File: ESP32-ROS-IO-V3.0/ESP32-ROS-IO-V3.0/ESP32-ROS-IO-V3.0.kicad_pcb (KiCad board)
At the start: 2 copper layers, 99.1 x 99.1 mm, 64 parts, among them J1 Conn_01x19_Socket, J12 XT60-M, J13 XT60-M, J2 Conn_01x19_Socket, J3 Conn_01x19_Socket, J4 Conn_01x19_Socket, SW1 SW1, SW2 SW2, SW3 SW3, SW4 SW4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

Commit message: 名前変更、整理
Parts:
- removed G***, G***5, G***6: LOGO, LOGO
- removed MD1: MD1, Connector_PinHeader_2.54mm:PinHeader_1x04_P2.54mm_Vertical
- removed MD2: MD2, Connector_PinHeader_2.54mm:PinHeader_1x04_P2.54mm_Vertical
- removed MD3: MD3, Connector_PinHeader_2.54mm:PinHeader_1x04_P2.54mm_Vertical
- removed MD4: MD4, Connector_PinHeader_2.54mm:PinHeader_1x04_P2.54mm_Vertical
- removed MD5: MD5, Connector_PinHeader_2.54mm:PinHeader_1x04_P2.54mm_Vertical
- removed MD6: MD6, Connector_PinHeader_2.54mm:PinHeader_1x04_P2.54mm_Vertical
- removed MD7: MD7, Connector_PinHeader_2.54mm:PinHeader_1x04_P2.54mm_Vertical
- removed MD8: MD8, Connector_PinHeader_2.54mm:PinHeader_1x04_P2.54mm_Vertical
- removed REF**1, REF**2, REF**3, REF**4: MountingHole_3.2mm_M3, MountingHole:MountingHole_3.2mm_M3
- removed Servo5: Servo5, Connector_JST:JST_XH_B3B-XH-A_1x03_P2.50mm_Vertical
- removed Servo6: Servo6, Connector_JST:JST_XH_B3B-XH-A_1x03_P2.50mm_Vertical
- removed Servo7: Servo7, Connector_JST:JST_XH_B3B-XH-A_1x03_P2.50mm_Vertical
- removed Servo8: Servo8, Connector_JST:JST_XH_B3B-XH-A_1x03_P2.50mm_Vertical
- added J5: Conn_01x02_Pin, Connector_PinSocket_2.54mm:PinSocket_1x19_P2.54mm_Vertical, F.Cu at (228.6, 94.2)
- added J6: Conn_01x02_Pin, Connector_PinSocket_2.54mm:PinSocket_1x19_P2.54mm_Vertical, F.Cu at (232.4, 94.2)
- J12, J13: footprint Connector_AMASS:AMASS_XT60-M_1x02_P7.20mm_Vertical -> XT60PW-M (2):AMASS_XT30PW-F
- moved SW4 159.6 mm to (31.3, 2.88)
- moved J13 149.6 mm to (21.8, 56.0)
- moved SW5 147.0 mm to (31.3, 10.7)
- moved SW6 147.0 mm to (31.3, 18.5)
- moved SW7 147.0 mm to (31.3, 26.3)
- moved SW8 147.0 mm to (31.3, 34.1)
- moved CAN_BUS8 141.2 mm to (12.4, 10.7), turned to 0 degrees
- moved SW1 139.2 mm to (21.9, 26.3)
- moved SW2 139.2 mm to (21.9, 34.1)
- moved SW3 139.2 mm to (21.9, 41.9)
- moved CAN_BUS7 137.9 mm to (12.4, 2.88), turned to 0 degrees
- moved SV7 136.8 mm to (21.9, 18.5), turned to 0 degrees
- moved VMD3/VMD4 136.1 mm to (44.2, 33.0), turned to 0 degrees
- moved SV6 133.9 mm to (21.9, 10.7), turned to 0 degrees
- moved D1 133.2 mm to (59.7, 46.1)
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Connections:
- ENC1 pad 3: GPIO12 -> GPIO19
- ENC1 pad 4: GPIO13 -> GPIO21
- ENC2 pad 3: GPIO14 -> GPIO22
- ENC2 pad 4: GPIO15 -> GPIO23
- ENC3 pad 3: GPIO21 -> GPIO15
- ENC3 pad 4: GPIO22 -> GPIO16
- ENC4 pad 3: GPIO23 -> GPIO17
- ENC4 pad 4: GPIO25 -> GPIO18
- J3 pad 13: GPIO4 -> CAN_TX
- J3 pad 15: GPIO2 -> CAN_RX
- J4 pad 13: GPIO4 -> CAN_TX
- J4 pad 15: GPIO2 -> CAN_RX
- SW1 pad 1: GPIO26 -> GPIO5
- SW2 pad 1: GPIO27 -> GPIO12
- SW3 pad 1: GPIO32 -> GPIO13
- SW4 pad 1: GPIO33 -> GPIO14
- SW5 pad 1: GPIO2 -> GPIO15
- SW6 pad 1: GPIO19 -> GPIO16
- SW7 pad 1: GPIO14 -> GPIO17
- SW8 pad 1: GPIO15 -> GPIO18
- Servo1 pad 1: GPIO16 -> GPIO19
- Servo2 pad 1: GPIO17 -> GPIO21
- Servo3 pad 1: GPIO18 -> GPIO22
- Servo4 pad 1: GPIO19 -> GPIO23
- U1 pad 1: GPIO5 -> CAN_TX
- U1 pad 4: GPIO4 -> CAN_RX
- U2 pad 1: GPIO2 -> GPIO25
- U2 pad 2: GPIO4 -> GPIO26
- U2 pad 3: GPIO5 -> GPIO27
- U2 pad 4: GPIO12 -> GPIO32
- U2 pad 5: GPIO13 -> GPIO33
- U2 pad 6: GPIO14 -> TR6
- U2 pad 7: GPIO15 -> TR6_Bypass_OUT
- VMD1/VMD2 pad 11: GPIO12 -> GPIO15
- VMD1/VMD2 pad 5: GPIO22 -> GPIO12
- VMD1/VMD2 pad 7: GPIO13 -> GPIO16
- VMD1/VMD2 pad 9: GPIO21 -> GPIO5
- VMD3/VMD4 pad 11: GPIO14 -> GPIO17
- VMD3/VMD4 pad 5: GPIO25 -> GPIO14
- VMD3/VMD4 pad 7: GPIO15 -> GPIO18
- VMD3/VMD4 pad 9: GPIO23 -> GPIO13
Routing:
- net (no net): track 0.00 -> 276.3 mm, vias 0 -> 4
- net GPIO2: track 129.3 -> 0.00 mm, vias 1 -> 0
- net GPIO4: track 120.0 -> 0.00 mm, vias 3 -> 0
- net GPIO22: track 203.0 -> 300.9 mm, vias 0 -> 1
- net GPIO18: track 97.9 -> 0.00 mm, vias 1 -> 0
- net GPIO21: track 189.7 -> 274.8 mm, vias 1 -> 2
- net GPIO19: track 153.2 -> 231.8 mm, vias 3 -> 5
- net GPIO23: track 152.3 -> 85.1 mm
- net GPIO13: track 162.0 -> 112.7 mm, vias 1 -> 0
- net GPIO15: track 195.2 -> 233.4 mm
- net GPIO12: track 152.2 -> 114.0 mm
- net GPIO16: track 78.6 -> 49.3 mm, vias 2 -> 1
- net +5V: track 27.0 -> 0.00 mm
- net GPIO17: track 85.1 -> 67.3 mm, vias 1 -> 0
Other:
- board outline removed
- board text removed: "+ GND"
- board text removed: "24V"
- board text removed: "3V G A B"
- board text removed: "5V G P D"
- board text removed: "CAN"
- board text removed: "ESP32-DevKitC V4"
- board text removed: "ESP32-IO-Board-V1.1 2025, NHK-Project, RRST"
- board text removed: "GND +"
- board text removed: "GND GND"
- board text removed: "H L"
- board text removed: "S + GND"
- board text removed: "VSRV"

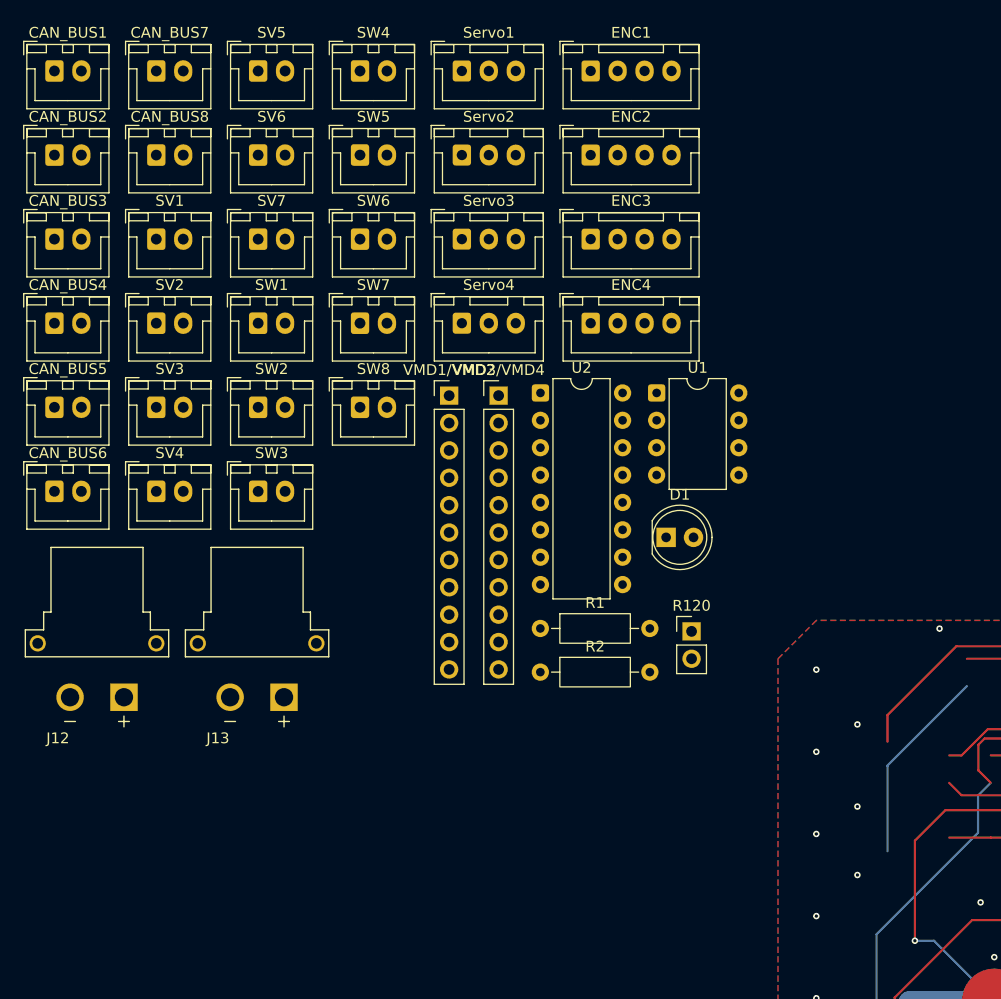
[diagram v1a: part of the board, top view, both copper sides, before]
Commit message: Gerberをzip形式に圧縮、発注したい
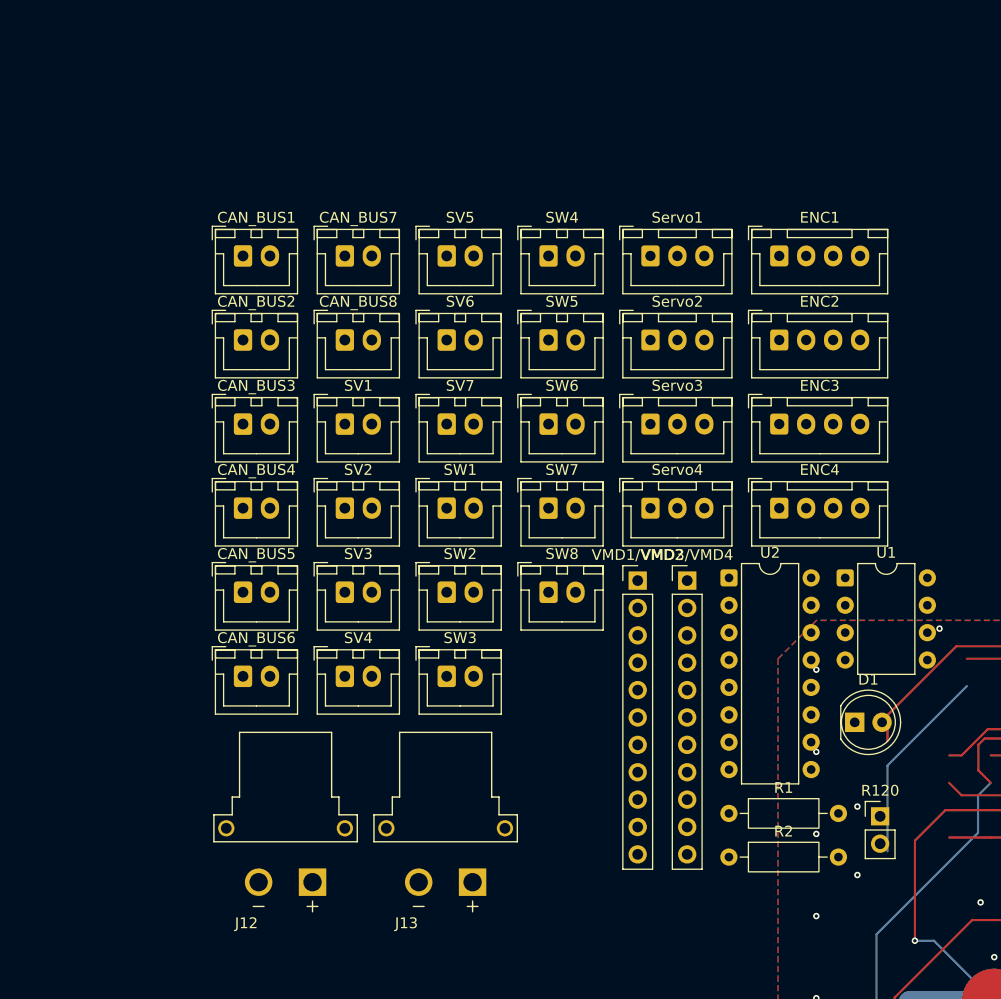
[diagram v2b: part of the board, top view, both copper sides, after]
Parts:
- moved U1 24.5 mm to (76.3, 49.9)
- moved U2 24.5 mm to (65.6, 49.9)
- moved VMD1/VMD2 24.5 mm to (57.1, 50.2)
- moved CAN_BUS7 24.5 mm to (29.9, 20.0)
- moved CAN_BUS8 24.5 mm to (29.9, 27.8)
- moved J12 24.5 mm to (24.4, 73.1)
- moved J13 24.5 mm to (39.3, 73.1)
- moved R1 24.5 mm to (65.5, 71.8)
- moved SV1 24.5 mm to (29.9, 35.6)
- moved SV2 24.5 mm to (29.9, 43.4)
- moved SV3 24.5 mm to (29.9, 51.2)
- moved SV4 24.5 mm to (29.9, 59.0)
- moved SW4 24.5 mm to (48.8, 20.0)
- moved SW5 24.5 mm to (48.8, 27.8)
- moved SW6 24.5 mm to (48.8, 35.6)
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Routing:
- net CANL: track 104.1 -> 32.4 mm
- net 3V3: track 84.0 -> 155.6 mm

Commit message: また変更したよ
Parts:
- removed VMD1/VMD2: VMD1/VMD2, Connector_PinHeader_2.54mm:PinHeader_1x11_P2.54mm_Vertical
- removed VMD3/VMD4: VMD3/VMD4, Connector_PinHeader_2.54mm:PinHeader_1x11_P2.54mm_Vertical
- added J10: XT30UPB-M, XT30UPB-M:AMASS_XT30UPB-M, F.Cu at (81.5, 32.6)
- added J11: XT30UPB-M, XT30UPB-M:AMASS_XT30UPB-M, F.Cu at (81.5, 39.3)
- added J14: XT60-M, XT60-M:AMASS_XT60-M, F.Cu at (83.7, 67.3)
- added J15: XT60-M, XT60-M:AMASS_XT60-M, F.Cu at (83.7, 77.0)
- added J7: Conn_01x04_Socket, Connector_PinSocket_2.54mm:PinSocket_1x04_P2.54mm_Vertical, F.Cu at (20.4, 76.5)
- added J8: XT30UPB-M, XT30UPB-M:AMASS_XT30UPB-M, F.Cu at (81.5, 19.1)
- added J9: XT30UPB-M, XT30UPB-M:AMASS_XT30UPB-M, F.Cu at (81.5, 25.8)
- J12, J13: value XT60-M -> XT30UPB-M; footprint XT60PW-M (2):AMASS_XT30PW-F -> XT30UPB-M:AMASS_XT30UPB-M
- J5, J6: footprint Connector_PinSocket_2.54mm:PinSocket_1x19_P2.54mm_Vertical -> Connector_PinHeader_2.54mm:PinHeader_1x02_P2.54mm_Vertical
- moved J3 206.0 mm to (29.6, 18.0)
- moved J4 205.3 mm to (34.2, 18.0)
- moved J1 191.1 mm to (20.4, 18.0)
- moved J2 183.4 mm to (25.0, 18.0)
- moved J5 153.0 mm to (75.9, 84.1)
- moved J6 152.2 mm to (80.5, 84.1)
- moved J12 63.2 mm to (81.5, 46.1)
- moved U1 58.4 mm to (24.2, 76.2)
- moved D1 58.4 mm to (25.1, 89.6)
- moved Servo4 49.4 mm to (39.9, 89.3)
- moved Servo1 49.4 mm to (39.9, 65.9)
- moved ENC4 49.4 mm to (51.9, 89.3)
- moved ENC1 49.4 mm to (51.9, 65.9)
- moved ENC2 49.4 mm to (51.9, 73.7)
- moved ENC3 49.4 mm to (51.9, 81.5)
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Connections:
- net 5V0 renamed 5V
- J12 pad N: GND -> GPIO17
- J12 pad P: SERVO+ -> GPIO13
- J13 pad N: GND -> GPIO18
- J13 pad P: +24V -> GPIO14
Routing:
- net GND: track 397.4 -> 0.00 mm, vias 111 -> 0
- net GPIO22: track 300.9 -> 0.00 mm, vias 1 -> 0
- net (no net): track 276.3 -> 0.00 mm, vias 4 -> 0
- net GPIO21: track 274.8 -> 0.00 mm, vias 2 -> 0
- net GPIO15: track 233.4 -> 0.00 mm, vias 1 -> 0
- net GPIO19: track 231.8 -> 0.00 mm, vias 5 -> 0
- net GPIO14: track 191.2 -> 0.00 mm, vias 1 -> 0
- net 3V3: track 155.6 -> 0.00 mm, vias 1 -> 0
- net GPIO25: track 155.6 -> 0.00 mm, vias 2 -> 0
- net SERVO+: track 134.2 -> 0.00 mm
- net +24V: track 121.3 -> 0.00 mm
- net GPIO12: track 114.0 -> 0.00 mm, vias 1 -> 0
- net GPIO13: track 112.7 -> 0.00 mm
- net GPIO26: track 108.4 -> 0.00 mm, vias 1 -> 0
- net GPIO27: track 107.6 -> 0.00 mm, vias 1 -> 0
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- removed copper zone on B.Cu, net GND
- removed copper zone on F.Cu, net GND

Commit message: 授業中続きやるよー
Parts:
- moved J3 218.5 mm to (228.6, 108.2)
- moved J1 200.5 mm to (199.4, 108.2)
- moved J4 124.3 mm to (148.1, 67.6)
- moved J2 124.3 mm to (138.9, 67.6)
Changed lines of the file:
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@@
 		)
 		(embedded_fonts no)
+		(model "${KIPRJMOD}/XT30UPB-M/XT30UPB-M.step"
+			(offset
+				(xyz 0 0 0)
+			)
+			(scale
+				(xyz 1 1 1)
+			)
+			(rotate
+				(xyz 90 -180 -180)
+			)
+		)
 	)
 	(footprint "Connector_JST:JST_XH_B2B-XH-A_1x02_P2.50mm_Vertical"
@@
 		)
 		(embedded_fonts no)
+		(model "C:/Users/minio/kicad-ws/MD/MDv3/XT60-M/XT60-M.step"
+			(offset
+				(xyz 0 0 0)
+			)
+			(scale
+				(xyz 1 1 1)
+			)
+			(rotate
+				(xyz 90 -180 -180)
+			)
+		)
 	)
 	(footprint "Connector_JST:JST_XH_B4B-XH-A_1x04_P2.50mm_Vertical"
@@
 		)
 		(embedded_fonts no)
+		(model "C:/Users/minio/kicad-ws/MD/MDv3/XT60-M/XT60-M.step"
+			(offset
+				(xyz 0 0 0)
+			)
+			(scale
+				(xyz 1 1 1)
+			)
+			(rotate
+				(xyz 90 -180 -180)
+			)
+		)
 	)
 	(footprint "Package_DIP:DIP-16_W7.62mm"
@@
 	(footprint "Connector_PinSocket_2.54mm:PinSocket_1x19_P2.54mm_Vertical"
 		(layer "F.Cu")
-		(at 24.96 18.004)
+		(at 138.91 67.564)
 		(descr "Through hole straight socket strip, 1x19, 2.54mm pitch, single row (from Kicad 4.0.7), script generated")
 		(tags "Through hole socket strip THT 1x19 2.54mm single row")
@@
 		)
 		(embedded_fonts no)
+		(model "${KIPRJMOD}/XT30UPB-M/XT30UPB-M.step"
+			(offset
+				(xyz 0 0 0)
+			)
+			(scale
+				(xyz 1 1 1)
+			)
+			(rotate
+				(xyz 90 180 -180)
+			)
+		)
 	)
 	(footprint "Connector_PinSocket_2.54mm:PinSocket_1x19_P2.54mm_Vertical"
 		(layer "F.Cu")
-		(at 29.56 18.004)
+		(at 228.6 108.204)
 		(descr "Through hole straight socket strip, 1x19, 2.54mm pitch, single row (from Kicad 4.0.7), script generated")
 		(tags "Through hole socket strip THT 1x19 2.54mm single row")
@@
 		)
 		(embedded_fonts no)
+		(model "${KIPRJMOD}/XT30UPB-M/XT30UPB-M.step"
+			(offset
+				(xyz 0 0 0)
+			)
+			(scale
+				(xyz 1 1 1)
+			)
+			(rotate
+				(xyz 90 -180 -180)
+			)
+		)
 	)
 	(footprint "Connector_PinSocket_2.54mm:PinSocket_1x19_P2.54mm_Vertical"
 		(layer "F.Cu")
-		(at 20.36 18.004)
+		(at 199.39 108.204)
 		(descr "Through hole straight socket strip, 1x19, 2.54mm pitch, single row (from Kicad 4.0.7), script generated")
 		(tags "Through hole socket strip THT 1x19 2.54mm single row")
@@
 		)
 		(embedded_fonts no)
+		(model "${KIPRJMOD}/XT30UPB-M/XT30UPB-M.step"
+			(offset
+				(xyz 0 0 0)
+			)
+			(scale
+				(xyz 1 1 1)
+			)
+			(rotate
+				(xyz 90 -180 180)
+			)
+		)
 	)
 	(footprint "Connector_PinSocket_2.54mm:PinSocket_1x19_P2.54mm_Vertical"
 		(layer "F.Cu")
-		(at 34.16 18.004)
+		(at 148.11 67.564)
 		(descr "Through hole straight socket strip, 1x19, 2.54mm pitch, single row (from Kicad 4.0.7), script generated")
 		(tags "Through hole socket strip THT 1x19 2.54mm single row")
@@
 		)
 		(embedded_fonts no)
+		(model "${KIPRJMOD}/XT30UPB-M/XT30UPB-M.step"
+			(offset
+				(xyz 0 0 0)
+			)
+			(scale
+				(xyz 1 1 1)
+			)
+			(rotate
+				(xyz 90 -180 -180)
+			)
+		)
 	)
 	(footprint "Connector_JST:JST_XH_B2B-XH-A_1x02_P2.50mm_Vertical"
@@
 		)
 		(embedded_fonts no)
+		(model "${KIPRJMOD}/XT30UPB-M/XT30UPB-M.step"
+			(offset
+				(xyz 0 0 0)
+			)
+			(scale
+				(xyz 1 1 1)
+			)
+			(rotate
+				(xyz 90 -180 -180)
+			)
+		)
 	)
 	(footprint "Connector_JST:JST_XH_B2B-XH-A_1x02_P2.50mm_Vertical"

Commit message: 発注元が空気を読んで私のミスを修正してくれますように
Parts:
- added J16: XT60-M, XT60-M:AMASS_XT60-M, F.Cu at (90.8, 78.3)
- added J17: XT60-M, XT60-M:AMASS_XT60-M, F.Cu at (90.8, 87.9)
- J10, J11, J12, J13, J8, J9: value XT30UPB-M -> XT30PW-F; footprint XT30UPB-M:AMASS_XT30UPB-M -> XT30PW-F:AMASS_XT30PW-F
- J14, J15: value XT60-M -> XT30PW-F; footprint XT60-M:AMASS_XT60-M -> XT30PW-F:AMASS_XT30PW-F
- moved J7 76.9 mm to (93.8, 53.9)
- moved D1 72.3 mm to (94.0, 67.6)
- moved J3 71.2 mm to (157.5, 105.7)
- moved J1 71.2 mm to (128.3, 105.7)
- moved J13 58.4 mm to (24.0, 43.3)
- moved J8 57.9 mm to (24.0, 25.3)
- moved R1 53.8 mm to (67.9, 91.9)
- moved R2 53.8 mm to (67.9, 96.0)
- moved J14 50.9 mm to (38.8, 43.3)
- moved J15 45.1 mm to (53.7, 43.3)
- moved J9 42.7 mm to (38.8, 25.3)
- moved J2 41.2 mm to (123.2, 105.7)
- moved CAN_BUS7 41.0 mm to (29.5, 55.0)
- moved SV5 41.0 mm to (38.9, 55.0)
- moved SW4 41.0 mm to (48.4, 55.0)
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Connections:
- J10 pad N: GPIO16 -> GND
- J10 pad P: GPIO12 -> GND
- J11 pad N: GND -> GPIO16
- J11 pad P: GND -> GPIO12
- J12 pad N: GPIO17 -> GND
- J12 pad P: GPIO13 -> GND
- J13 pad N: GPIO18 -> GPIO17
- J13 pad P: GPIO14 -> GPIO13
- J14 pad N: GND -> GPIO18
- J14 pad P: SERVO+ -> GPIO14
- J15 pad P: +24V -> GND

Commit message: え四方にMD乗せるってことですか？たしろさん
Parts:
- moved J8 199.2 mm to (182.9, 145.5), turned to -90 degrees
- moved J9 179.0 mm to (182.9, 131.6), turned to -90 degrees
- moved J14 154.7 mm to (136.0, 163.6), turned to 180 degrees
- moved J15 138.0 mm to (121.1, 163.6), turned to 180 degrees
- moved J10 121.1 mm to (160.4, 82.3)
- moved J11 121.1 mm to (175.3, 82.3)
- moved J13 111.0 mm to (108.8, 114.9), turned to 90 degrees
- moved J12 79.9 mm to (108.8, 101.0), turned to 90 degrees

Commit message: なんでXTの位置間合わないんだ、だるい
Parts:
- J10, J11, J12, J13, J14, J15, J8, J9: value XT30PW-F -> XT30UPB-F; footprint XT30PW-F:AMASS_XT30PW-F -> XT30UPB-F:AMASS_XT30U-F_1x02_P5.0mm_Vertical
- moved J8 108.0 mm to (86.1, 97.6), turned to 0 degrees
- moved J9 100.4 mm to (86.1, 104.9), turned to 0 degrees
- moved J11 96.6 mm to (86.1, 119.4)
- moved J10 80.1 mm to (86.1, 112.1)
- moved J14 54.7 mm to (86.1, 141.1), turned to 0 degrees
- moved J15 38.2 mm to (86.1, 148.4), turned to 0 degrees
- moved J12 34.3 mm to (86.1, 126.6), turned to 0 degrees
- moved J13 29.7 mm to (86.1, 133.9), turned to 0 degrees

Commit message: (T_T)
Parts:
- moved J10 0.68 mm to (85.7, 111.6)
- moved J11 0.68 mm to (85.7, 118.8)
- moved J12 0.68 mm to (85.7, 126.1)
- moved J13 0.68 mm to (85.7, 133.3)
- moved J14 0.68 mm to (85.7, 140.6)
- moved J15 0.68 mm to (85.7, 147.8)
- moved J8 0.68 mm to (85.7, 97.1)
- moved J9 0.68 mm to (85.7, 104.3)
